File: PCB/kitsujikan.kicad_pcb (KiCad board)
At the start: 2 copper layers, 65 x 90 mm, 23 parts, among them J1 Battery, J2 XIAO_BAT, J3 OLED_SSD1306, Q1 2N3904, SW1 Power, SW2 30min, SW3 60min, SW4 90min, SW5 OK_GREEN, SW6 NO_RED, U1 XIAO-ESP32-C3-SMD

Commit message: week 1: fix wiring route
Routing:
- net /BTN_30: track 130.4 -> 129.0 mm
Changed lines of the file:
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@@
 	)
 	(segment
-		(start 87 57)
-		(end 87 97)
+		(start 88 98)
+		(end 88.5 98)
 		(width 0.2)
 		(layer "B.Cu")
@@
 	)
 	(segment
-		(start 146 57)
+		(start 147 57)
 		(end 87 57)
+		(width 0.2)
+		(layer "B.Cu")
+		(net "/BTN_30")
+	)
+	(segment
+		(start 147.08 57.08)
+		(end 147 57)
 		(width 0.2)
 		(layer "B.Cu")
@@
 	)
 	(segment
-		(start 147 56)
-		(end 146 57)
-		(width 0.2)
-		(layer "B.Cu")
-		(net "/BTN_30")
-	)
-	(segment
-		(start 147.08 56.08)
-		(end 147 56)
+		(start 87 57)
+		(end 87 97)
 		(width 0.2)
 		(layer "B.Cu")
@@
 	(segment
 		(start 147.08 61)
-		(end 147.08 56.08)
+		(end 147.08 57.08)
 		(width 0.2)
 		(layer "B.Cu")
-		(net "/BTN_30")
-	)
-	(segment
-		(start 88 98)
-		(end 88.5 98)
-		(width 0.2)
-		(layer "B.Cu")

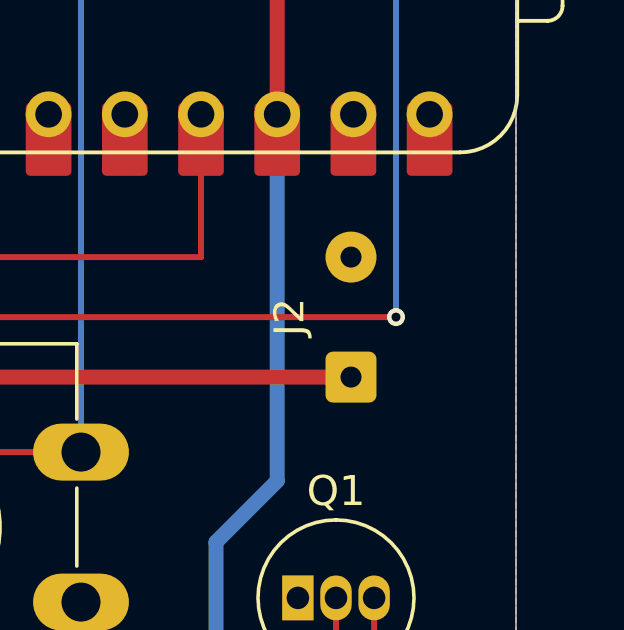
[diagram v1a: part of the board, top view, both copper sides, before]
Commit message: week 1: BAT+/BAT- silkscreen label
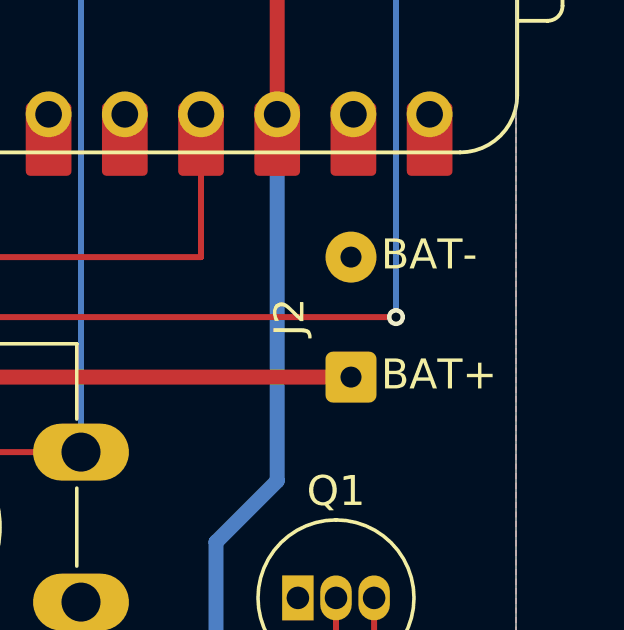
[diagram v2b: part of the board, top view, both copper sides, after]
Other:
- board text added: "BAT+"
- board text added: "BAT-"
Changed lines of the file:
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@@
 		(layer "Edge.Cuts")
+	)
+	(gr_text "BAT-"
+		(at 145.5 92 0)
+		(layer "F.SilkS")
+		(effects
+			(font
+				(size 1 1)
+				(thickness 0.1)
+			)
+			(justify left bottom)
+		)
+	)
+	(gr_text "BAT+"
+		(at 145.5 96 0)
+		(layer "F.SilkS")
+		(effects
+			(font
+				(size 1 1)
+				(thickness 0.1)
+			)
+			(justify left bottom)
+		)
 	)
 	(segment

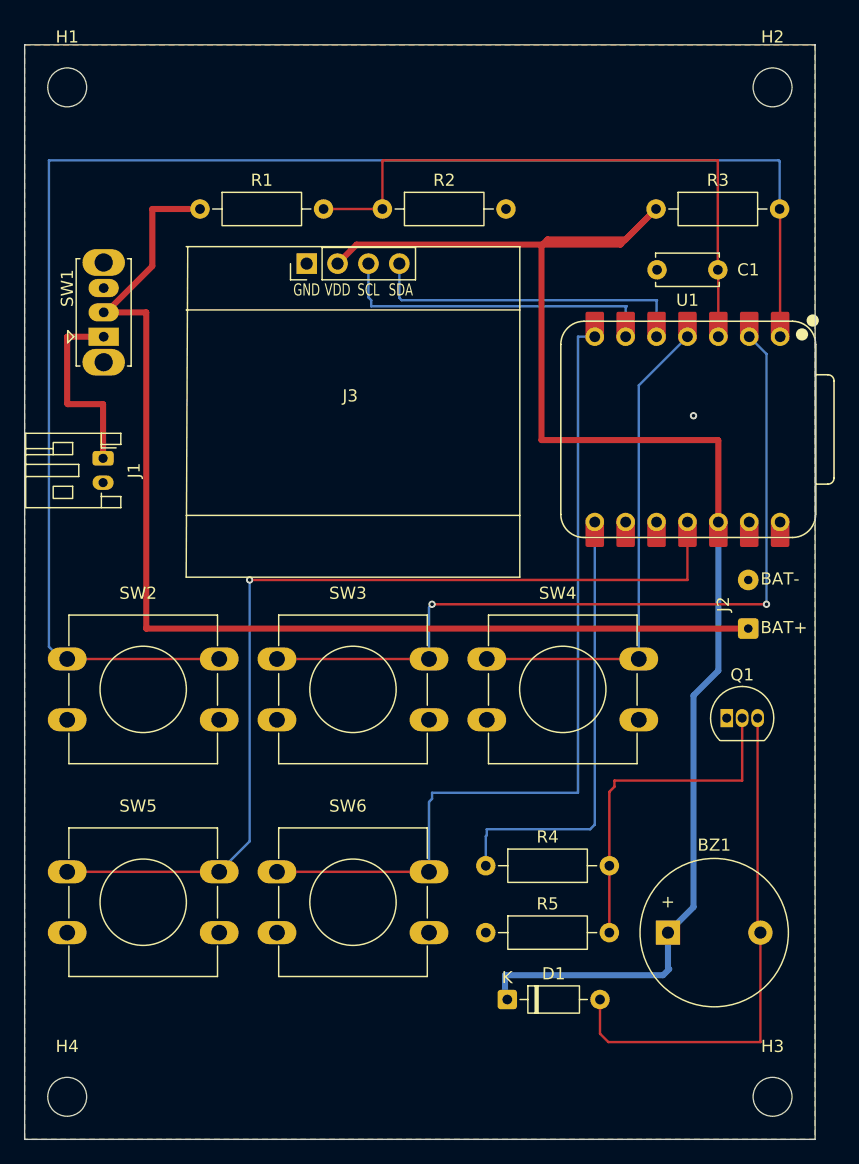
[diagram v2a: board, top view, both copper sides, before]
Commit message: week 1: silkscreen label update
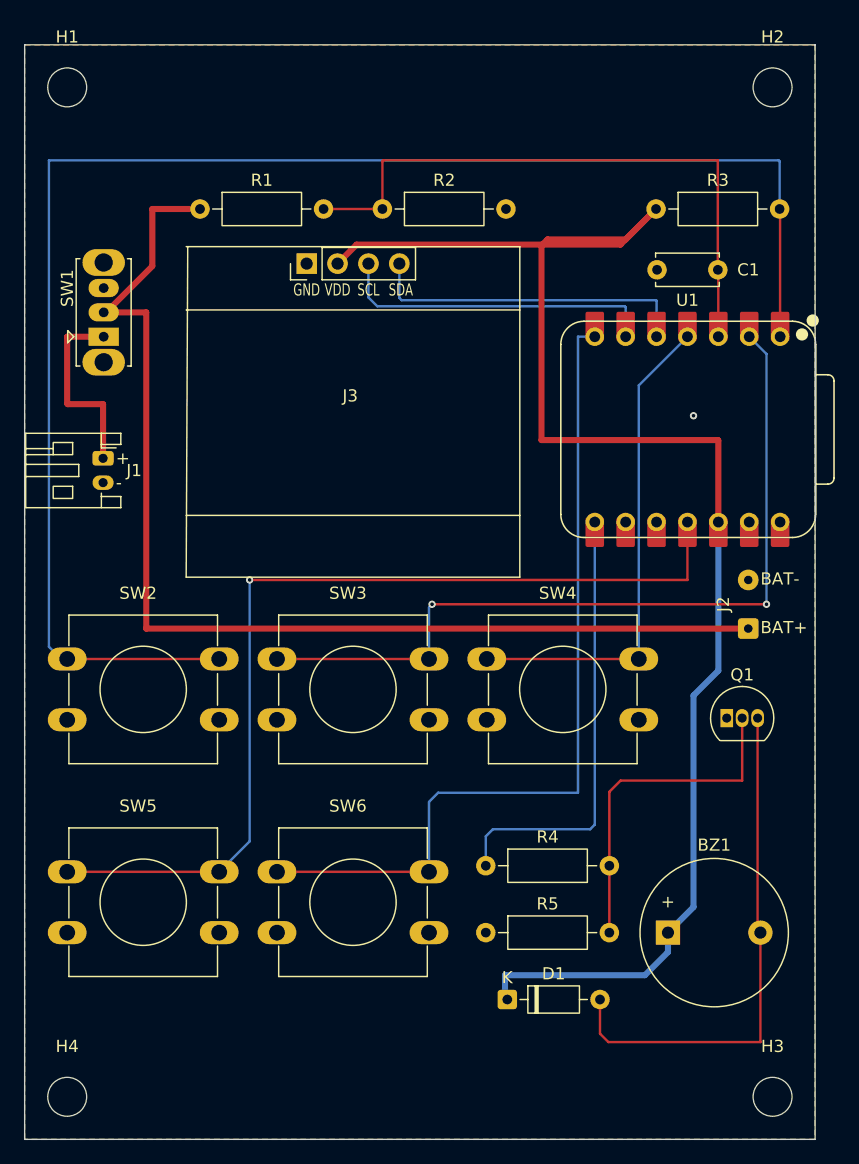
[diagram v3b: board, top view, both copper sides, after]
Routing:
- net +3.3V: track 130.3 -> 129.3 mm
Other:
- board text added: "+"
- board text added: "-"
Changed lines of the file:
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@@
 		(tags "connector JST PH horizontal")
 		(property "Reference" "J1"
-			(at 1 -2.55 90)
+			(at 1 -2.55 180)
 			(layer "F.SilkS")
 			(effects
@@
 		(layer "Edge.Cuts")
 	)
+	(gr_text "+"
+		(at 92.5 81.5 0)
+		(layer "F.SilkS")
+		(effects
+			(font
+				(size 1 1)
+				(thickness 0.1)
+			)
+			(justify left)
+		)
+	)
+	(gr_text "-"
+		(at 92.5 83.5 0)
+		(layer "F.SilkS")
+		(effects
+			(font
+				(size 1 1)
+				(thickness 0.1)
+			)
+			(justify left)
+		)
+	)
 	(gr_text "BAT-"
 		(at 145.5 92 0)
@@
 	)
 	(segment
+		(start 131.5 112)
+		(end 123.5 112)
+		(width 0.2)
+		(layer "B.Cu")
+		(net "/BUZZER")
+	)
+	(segment
+		(start 131.88 111.62)
+		(end 131.5 112)
+		(width 0.2)
+		(layer "B.Cu")
+		(net "/BUZZER")
+	)
+	(segment
+		(start 123.5 112)
+		(end 122.92 112.58)
+		(width 0.2)
+		(layer "B.Cu")
+		(net "/BUZZER")
+	)
+	(segment
+		(start 122.92 112.58)
+		(end 122.92 115)
+		(width 0.2)
+		(layer "B.Cu")
+		(net "/BUZZER")
+	)
+	(segment
 		(start 131.88 86.74)
 		(end 131.88 111.62)
@@
 	)
 	(segment
-		(start 122.92 112.58)
-		(end 122.92 115)
-		(width 0.2)
-		(layer "B.Cu")
-		(net "/BUZZER")
-	)
-	(segment
-		(start 123 112.5)
-		(end 122.92 112.58)
-		(width 0.2)
-		(layer "B.Cu")
-		(net "/BUZZER")
-	)
-	(segment
-		(start 123 112)
-		(end 123 112.5)
-		(width 0.2)
-		(layer "B.Cu")
-		(net "/BUZZER")
-	)
-	(segment
-		(start 131.88 111.62)
-		(end 131.5 112)
-		(width 0.2)
-		(layer "B.Cu")
-		(net "/BUZZER")
-	)
-	(segment
-		(start 131.5 112)
-		(end 123 112)
-		(width 0.2)
-		(layer "B.Cu")
-		(net "/BUZZER")
-	)
-	(segment
-		(start 133.5 108)
-		(end 133.5 108.5)
-		(width 0.2)
-		(layer "F.Cu")
-		(net "Net-(Q1-B)")
-	)
-	(segment
-		(start 133.5 108.5)
-		(end 133.08 108.92)
-		(width 0.2)
-		(layer "F.Cu")
-		(net "Net-(Q1-B)")
-	)
-	(segment
-		(start 144 108)
-		(end 133.5 108)
+		(start 133.08 108.92)
+		(end 133.08 115)
 		(width 0.2)
 		(layer "F.Cu")
@@
 	)
 	(segment
+		(start 134 108)
+		(end 133.08 108.92)
+		(width 0.2)
+		(layer "F.Cu")
+		(net "Net-(Q1-B)")
+	)
+	(segment
+		(start 144 108)
+		(end 134 108)
+		(width 0.2)
+		(layer "F.Cu")
+		(net "Net-(Q1-B)")
+	)
+	(segment
 		(start 133.08 115)
 		(end 133.08 120.5)
@@
 	)
 	(segment
-		(start 133.08 108.92)
-		(end 133.08 115)
-		(width 0.2)
-		(layer "F.Cu")
-		(net "Net-(Q1-B)")
-	)
-	(segment
 		(start 105.75 115.5)
 		(end 118.25 115.5)
@@
 	)
 	(segment
+		(start 130.5 109)
+		(end 119 109)
+		(width 0.2)
+		(layer "B.Cu")
+		(net "/BTN_NO")
+	)
+	(segment
+		(start 119 109)
+		(end 118.25 109.75)
+		(width 0.2)
+		(layer "B.Cu")
+		(net "/BTN_NO")
+	)
+	(segment
 		(start 131.88 71.5)
 		(end 130.5 71.5)
@@
 	)
 	(segment
-		(start 118.5 109.5)
-		(end 118.25 109.75)
+		(start 118.25 109.75)
+		(end 118.25 115.5)
 		(width 0.2)
 		(layer "B.Cu")
@@
 		(start 130.5 71.5)
 		(end 130.5 109)
-		(width 0.2)
-		(layer "B.Cu")
-		(net "/BTN_NO")
-	)
-	(segment
-		(start 130.5 109)
-		(end 118.5 109)
-		(width 0.2)
-		(layer "B.Cu")
-		(net "/BTN_NO")
-	)
-	(segment
-		(start 118.5 109)
-		(end 118.5 109.5)
-		(width 0.2)
-		(layer "B.Cu")
-		(net "/BTN_NO")
-	)
-	(segment
-		(start 118.25 109.75)
-		(end 118.25 115.5)
 		(width 0.2)
 		(layer "B.Cu")
@@
 	)
 	(segment
-		(start 137.5 124)
+		(start 136 124)
 		(end 124.5 124)
 		(width 0.5)
@@
 	)
 	(segment
-		(start 138 123.5)
-		(end 137.5 124)
-		(width 0.5)
-		(layer "B.Cu")
-		(net "+3.3V")
-	)
-	(segment
 		(start 140 118.4)
 		(end 137.9 120.5)
@@
 	)
 	(segment
-		(start 137.9 120.5)
-		(end 137.9 123.4)
+		(start 124.5 124)
+		(end 124.5 125.81)
 		(width 0.5)
 		(layer "B.Cu")
@@
 	)
 	(segment
-		(start 137.9 123.4)
-		(end 138 123.5)
+		(start 137.9 122.1)
+		(end 136 124)
 		(width 0.5)
 		(layer "B.Cu")
@@
 	)
 	(segment
-		(start 124.5 124)
-		(end 124.5 125.81)
+		(start 137.9 120.5)
+		(end 137.9 122.1)
 		(width 0.5)
 		(layer "B.Cu")
@@
 	)
 	(segment
-		(start 113.5 68.5)
+		(start 134.34 69)
+		(end 114 69)
+		(width 0.2)
+		(layer "B.Cu")
+		(net "/SCL")
+	)
+	(segment
+		(start 114 69)
 		(end 113.27 68.27)
+		(width 0.2)
+		(layer "B.Cu")
+		(net "/SCL")
+	)
+	(segment
+		(start 113.27 68.27)
+		(end 113.27 65.492)
 		(width 0.2)
 		(layer "B.Cu")
@@
 	)
 	(segment
-		(start 113.27 68.27)
-		(end 113.27 65.492)
+		(start 134.42 69.08)
+		(end 134.34 69)
 		(width 0.2)
 		(layer "B.Cu")
@@
 	)
 	(segment
-		(start 134.42 69.08)
-		(end 134.5 69)
-		(width 0.2)
-		(layer "B.Cu")
-		(net "/SCL")
-	)
-	(segment
-		(start 134.5 69)
-		(end 113.5 69)
-		(width 0.2)
-		(layer "B.Cu")
-		(net "/SCL")
-	)
-	(segment
-		(start 113.5 69)
-		(end 113.5 68.5)
-		(width 0.2)
-		(layer "B.Cu")
-		(net "/SCL")
+		(start 136.92 68.5)
+		(end 116 68.5)
+		(width 0.2)
+		(layer "B.Cu")
+		(net "/SDA")
+	)
+	(segment
+		(start 115.81 68.31)
+		(end 115.81 65.492)
+		(width 0.2)
+		(layer "B.Cu")
+		(net "/SDA")
+	)
+	(segment
+		(start 136.96 68.54)
+		(end 136.92 68.5)
+		(width 0.2)
+		(layer "B.Cu")
+		(net "/SDA")
+	)
+	(segment
+		(start 116 68.5)
+		(end 115.81 68.31)
+		(width 0.2)
+		(layer "B.Cu")
+		(net "/SDA")
 	)
 	(segment
@@
 		(width 0.2)
 		(layer "B.Cu")
-		(net "/SDA")
-	)
-	(segment
-		(start 137 68.5)
-		(end 116 68.5)
-		(width 0.2)
-		(layer "B.Cu")
-		(net "/SDA")
-	)
-	(segment
-		(start 136.96 68.54)
-		(end 137 68.5)
-		(width 0.2)
-		(layer "B.Cu")
-		(net "/SDA")
-	)
-	(segment
-		(start 115.81 68.31)
-		(end 115.81 65.492)
-		(width 0.2)
-		(layer "B.Cu")
-		(net "/SDA")
-	)
-	(segment
-		(start 116 68.5)
-		(end 115.81 68.31)
-		(width 0.2)
-		(layer "B.Cu")

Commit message: week 1: silkscreen labels
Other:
- board text removed: "BAT+"
- board text removed: "BAT-"
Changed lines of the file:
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@@
 			(at 0 -4.15 0)
 			(layer "F.SilkS")
+			(hide yes)
 			(effects
 				(font
@@
 			(at 0 -4.15 0)
 			(layer "F.SilkS")
+			(hide yes)
 			(effects
 				(font
@@
 			(at 0 -4.15 0)
 			(layer "F.SilkS")
+			(hide yes)
 			(effects
 				(font
@@
 		(tags "connector JST PH horizontal")
 		(property "Reference" "J1"
-			(at 1 -2.55 180)
+			(at 5.5 2.45 180)
 			(layer "F.SilkS")
 			(effects
@@
 			(at 0 -4.15 0)
 			(layer "F.SilkS")
+			(hide yes)
 			(effects
 				(font
@@
 		)
 	)
-	(gr_text "BAT-"
-		(at 145.5 92 0)
+	(gr_text "-"
+		(at 146 92 0)
 		(layer "F.SilkS")
 		(effects
@@
 		)
 	)
-	(gr_text "BAT+"
-		(at 145.5 96 0)
+	(gr_text "+"
+		(at 146 96 0)
 		(layer "F.SilkS")
 		(effects
